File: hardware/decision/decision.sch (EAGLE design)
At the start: 3 parts

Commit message: update schematics
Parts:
- removed LM7805: 7805T, linear:7805T
- removed U$1: LCD-G12864FULL, SparkFun-Displays:LCD-G12864FULL
- added IC1: 7805T, linear:7805T
- added IC2: A1301UA, allegro:A1301UA
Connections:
- removed net P1.0: U$1.RST
- removed net P1.1: U$1.CS1
- removed net P1.4: U$1.DB1
- removed net P1.5: U$1.DB0
- removed net P2.5: U$1.E
- removed net P3.0: U$1.DB7
- removed net P3.1: U$1.DB6
- removed net P3.2: U$1.DB5
- removed net P3.3: U$1.DB4
- removed net P3.4: U$1.DB2
- removed net P4.2: U$1.R/W
- removed net P4.3: U$1.D/I
- removed net P4.7: U$1.DB3
- net GND: now also IC1.GND, IC2.GND; no longer BAT1.V-, LM7805.GND, U$1.K, U$1.VSS
- net N$1: now also IC1.VI; no longer LM7805.VI
- net P1.2: now also IC2.OUT; no longer U$1.CS2
- net VCC: now also IC1.VO, IC2.VCC; no longer LM7805.VO, U$1.A, U$1.VDD, U$1.VEE, U$1.VO
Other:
- note added: "Connects the Hall Effect Sensor to the Green Board and provides the Green Board with power"
- note added: "Derailleurs Decision Board Foster McLane"
- note added: "Hall Effect Sensor"
- note added: "LM7805"
- note removed: "Connects LCD to Green Board and supplies power to the Green Board"
- note removed: "Derailleurs Interface Board Foster McLane"
- note removed: "LCD 128x64"
- note removed: "Power Supply"
- moved on the sheet: BAT1
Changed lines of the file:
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@@
 </classes>
 <parts>
-<part name="U$1" library="SparkFun-Displays" deviceset="LCD-G12864" device="FULL"/>
 <part name="BAT1" library="SparkFun-Connectors" deviceset="BC9VPC" device=""/>
-<part name="LM7805" library="linear" deviceset="78*" device="T" technology="05"/>
+<part name="IC1" library="linear" deviceset="78*" device="T" technology="05"/>
+<part name="IC2" library="allegro" deviceset="A13*?" device="UA" technology="01"/>
 </parts>
 <sheets>
 <sheet>
 <plain>
-<text x="96.52" y="121.92" size="1.778" layer="97">LCD 128x64</text>
-<text x="25.4" y="109.22" size="1.778" layer="97">5V Voltage Regulator</text>
-<text x="-5.08" y="119.38" size="1.778" layer="97">Power Supply</text>
-<frame x1="-20.32" y1="35.56" x2="124.46" y2="154.94" columns="8" rows="5" layer="91"/>
-<text x="-10.16" y="144.78" size="1.778" layer="97">Connects LCD to Green Board and supplies power to the Green Board</text>
-<text x="-10.16" y="139.7" size="1.778" layer="97">This board connects to the Green Board via mated headers.</text>
-<text x="99.06" y="43.18" size="1.778" layer="97">Derailleurs
-Interface Board
+<text x="45.72" y="27.94" size="1.778" layer="97">LM7805</text>
+<frame x1="-2.54" y1="-20.32" x2="96.52" y2="63.5" columns="8" rows="5" layer="91"/>
+<text x="43.18" y="55.88" size="1.778" layer="97">Hall Effect Sensor</text>
+<text x="45.72" y="12.7" size="1.778" layer="97">5V Voltage Regulator</text>
+<text x="5.08" y="-5.08" size="1.778" layer="97">Connects the Hall Effect Sensor to the Green Board and provides
+the Green Board with power</text>
+<text x="5.08" y="-10.16" size="1.778" layer="97">This board connects to the Green Board via mated headers.</text>
+<text x="73.66" y="-15.24" size="1.778" layer="97">Derailleurs
+Decision Board
 Foster McLane</text>
 </plain>
 <instances>
-<instance part="U$1" gate="G$1" x="101.6" y="93.98"/>
-<instance part="BAT1" gate="G$1" x="0" y="96.52"/>
-<instance part="LM7805" gate="A1" x="20.32" y="104.14"/>
+<instance part="BAT1" gate="G$1" x="17.78" y="15.24"/>
+<instance part="IC1" gate="A1" x="43.18" y="22.86"/>
+<instance part="IC2" gate="G$1" x="43.18" y="48.26"/>
 </instances>
 <busses>
 </busses>
 <nets>
-<net name="P2.5" class="0">
+<net name="N$1" class="0">
 <segment>
-<pinref part="U$1" gate="G$1" pin="E"/>
-<wire x1="88.9" y1="76.2" x2="76.2" y2="76.2" width="0.1524" layer="91"/>
-<label x="76.2" y="76.2" size="1.778" layer="95" rot="R180" xref="yes"/>
+<pinref part="BAT1" gate="G$1" pin="V+"/>
+<pinref part="IC1" gate="A1" pin="VI"/>
+<wire x1="17.78" y1="22.86" x2="33.02" y2="22.86" width="0.1524" layer="91"/>
 </segment>
 </net>
-<net name="P4.3" class="0">
+<net name="GND" class="0">
 <segment>
-<pinref part="U$1" gate="G$1" pin="D/I"/>
-<wire x1="88.9" y1="78.74" x2="66.04" y2="78.74" width="0.1524" layer="91"/>
-<label x="66.04" y="78.74" size="1.778" layer="95" rot="R180" xref="yes"/>
+<pinref part="IC1" gate="A1" pin="GND"/>
+<wire x1="43.18" y1="15.24" x2="43.18" y2="5.08" width="0.1524" layer="91"/>
+<wire x1="43.18" y1="5.08" x2="17.78" y2="5.08" width="0.1524" layer="91"/>
+<wire x1="17.78" y1="5.08" x2="17.78" y2="7.62" width="0.1524" layer="91"/>
+<wire x1="43.18" y1="5.08" x2="60.96" y2="5.08" width="0.1524" layer="91"/>
+<label x="60.96" y="5.08" size="1.778" layer="95" xref="yes"/>
+</segment>
+<segment>
+<pinref part="IC2" gate="G$1" pin="GND"/>
+<wire x1="50.8" y1="45.72" x2="68.58" y2="45.72" width="0.1524" layer="91"/>
+<label x="68.58" y="45.72" size="1.778" layer="95" xref="yes"/>
 </segment>
 </net>
-<net name="P4.2" class="0">
+<net name="VCC" class="0">
 <segment>
-<pinref part="U$1" gate="G$1" pin="R/W"/>
-<wire x1="88.9" y1="81.28" x2="76.2" y2="81.28" width="0.1524" layer="91"/>
-<label x="76.2" y="81.28" size="1.778" layer="95" rot="R180" xref="yes"/>
+<pinref part="IC1" gate="A1" pin="VO"/>
+<wire x1="53.34" y1="22.86" x2="60.96" y2="22.86" width="0.1524" layer="91"/>
+<label x="60.96" y="22.86" size="1.778" layer="95" xref="yes"/>
 </segment>
-</net>
-<net name="P1.0" class="0">
 <segment>
-<pinref part="U$1" gate="G$1" pin="RST"/>
-<wire x1="88.9" y1="83.82" x2="66.04" y2="83.82" width="0.1524" layer="91"/>
-<label x="66.04" y="83.82" size="1.778" layer="95" rot="R180" xref="yes"/>
-</segment>
-</net>
-<net name="P1.1" class="0">
-<segment>
-<pinref part="U$1" gate="G$1" pin="CS1"/>
-<wire x1="88.9" y1="86.36" x2="76.2" y2="86.36" width="0.1524" layer="91"/>
-<label x="76.2" y="86.36" size="1.778" layer="95" rot="R180" xref="yes"/>
+<pinref part="IC2" gate="G$1" pin="VCC"/>
+<wire x1="50.8" y1="50.8" x2="68.58" y2="50.8" width="0.1524" layer="91"/>
+<label x="68.58" y="50.8" size="1.778" layer="95" xref="yes"/>
 </segment>
 </net>
 <net name="P1.2" class="0">
 <segment>
-<pinref part="U$1" gate="G$1" pin="CS2"/>
-<wire x1="88.9" y1="88.9" x2="66.04" y2="88.9" width="0.1524" layer="91"/>
-<label x="66.04" y="88.9" size="1.778" layer="95" rot="R180" xref="yes"/>
+<pinref part="IC2" gate="G$1" pin="OUT"/>
+<wire x1="50.8" y1="48.26" x2="58.42" y2="48.26" width="0.1524" layer="91"/>
+<label x="58.42" y="48.26" size="1.778" layer="95" xref="yes"/>
 </segment>
 </net>
-<net name="P3.0" class="0">
-<segment>
-<pinref part="U$1" gate="G$1" pin="DB7"/>
-<wire x1="88.9" y1="91.44" x2="76.2" y2="91.44" width="0.1524" layer="91"/>
-<label x="76.2" y="91.44" size="1.778" layer="95" rot="R180" xref="yes"/>
-</segment>
-</net>
-<net name="P3.1" class="0">
-<segment>
-<pinref part="U$1" gate="G$1" pin="DB6"/>
-<wire x1="88.9" y1="93.98" x2="66.04" y2="93.98" width="0.1524" layer="91"/>
-<label x="66.04" y="93.98" size="1.778" layer="95" rot="R180" xref="yes"/>
-</segment>
-</net>
-<net name="P3.2" class="0">
-<segment>
-<pinref part="U$1" gate="G$1" pin="DB5"/>
-<wire x1="88.9" y1="96.52" x2="76.2" y2="96.52" width="0.1524" layer="91"/>
-<label x="76.2" y="96.52" size="1.778" layer="95" rot="R180" xref="yes"/>
-</segment>
-</net>
-<net name="P3.3" class="0">
-<segment>
-<pinref part="U$1" gate="G$1" pin="DB4"/>
-<wire x1="88.9" y1="99.06" x2="66.04" y2="99.06" width="0.1524" layer="91"/>
-<label x="66.04" y="99.06" size="1.778" layer="95" rot="R180" xref="yes"/>
-</segment>
-</net>
-<net name="P4.7" class="0">
-<segment>
-<pinref part="U$1" gate="G$1" pin="DB3"/>
-<wire x1="88.9" y1="101.6" x2="76.2" y2="101.6" width="0.1524" layer="91"/>
-<label x="76.2" y="101.6" size="1.778" layer="95" rot="R180" xref="yes"/>
-</segment>
-</net>
-<net name="P3.4" class="0">
-<segment>
-<pinref part="U$1" gate="G$1" pin="DB2"/>
-<wire x1="88.9" y1="104.14" x2="66.04" y2="104.14" width="0.1524" layer="91"/>
-<label x="66.04" y="104.14" size="1.778" layer="95" rot="R180" xref="yes"/>
-</segment>
-</net>
-<net name="P1.4" class="0">
-<segment>
-<pinref part="U$1" gate="G$1" pin="DB1"/>
-<wire x1="88.9" y1="106.68" x2="76.2" y2="106.68" width="0.1524" layer="91"/>
-<label x="76.2" y="106.68" size="1.778" layer="95" rot="R180" xref="yes"/>
-</segment>
-</net>
-<net name="P1.5" class="0">
-<segment>
-<pinref part="U$1" gate="G$1" pin="DB0"/>
-<wire x1="88.9" y1="109.22" x2="66.04" y2="109.22" width="0.1524" layer="91"/>
-<label x="66.04" y="109.22" size="1.778" layer="95" rot="R180" xref="yes"/>
-</segment>
-</net>
-<net name="GND" class="0">
-<segment>
-<pinref part="U$1" gate="G$1" pin="VSS"/>
-<label x="66.04" y="114.3" size="1.778" layer="95" rot="R180" xref="yes"/>
-<wire x1="88.9" y1="114.3" x2="66.04" y2="114.3" width="0.1524" layer="91"/>
-</segment>
-<segment>
-<pinref part="U$1" gate="G$1" pin="K"/>
-<wire x1="88.9" y1="68.58" x2="66.04" y2="68.58" width="0.1524" layer="91"/>
-<label x="66.04" y="68.58" size="1.778" layer="95" rot="R180" xref="yes"/>
-</segment>
-<segment>
-<pinref part="LM7805" gate="A1" pin="GND"/>
-<wire x1="20.32" y1="96.52" x2="20.32" y2="83.82" width="0.1524" layer="91"/>
-<pinref part="BAT1" gate="G$1" pin="V-"/>
-<wire x1="20.32" y1="83.82" x2="12.7" y2="83.82" width="0.1524" layer="91"/>
-<wire x1="12.7" y1="83.82" x2="0" y2="83.82" width="0.1524" layer="91"/>
-<wire x1="0" y1="83.82" x2="0" y2="86.36" width="0.1524" layer="91"/>
-<wire x1="12.7" y1="83.82" x2="12.7" y2="88.9" width="0.1524" layer="91"/>
-<label x="12.7" y="88.9" size="1.778" layer="95" rot="R90" xref="yes"/>
-</segment>
-</net>
-<net name="VCC" class="0">
-<segment>
-<pinref part="U$1" gate="G$1" pin="VDD"/>
-<wire x1="88.9" y1="116.84" x2="76.2" y2="116.84" width="0.1524" layer="91"/>
-<label x="76.2" y="116.84" size="1.778" layer="95" rot="R180" xref="yes"/>
-</segment>
-<segment>
-<pinref part="U$1" gate="G$1" pin="VO"/>
-<wire x1="88.9" y1="111.76" x2="76.2" y2="111.76" width="0.1524" layer="91"/>
-<label x="76.2" y="111.76" size="1.778" layer="95" rot="R180" xref="yes"/>
-</segment>
-<segment>
-<pinref part="U$1" gate="G$1" pin="VEE"/>
-<wire x1="88.9" y1="73.66" x2="66.04" y2="73.66" width="0.1524" layer="91"/>
-<label x="66.04" y="73.66" size="1.778" layer="95" rot="R180" xref="yes"/>
-</segment>
-<segment>
-<pinref part="U$1" gate="G$1" pin="A"/>
-<wire x1="88.9" y1="71.12" x2="76.2" y2="71.12" width="0.1524" layer="91"/>
-<label x="76.2" y="71.12" size="1.778" layer="95" rot="R180" xref="yes"/>
-</segment>
-<segment>
-<pinref part="LM7805" gate="A1" pin="VO"/>
-<wire x1="30.48" y1="104.14" x2="38.1" y2="104.14" width="0.1524" layer="91"/>
-<label x="38.1" y="104.14" size="1.778" layer="95" xref="yes"/>
-</segment>
-</net>
-<net name="N$1" class="0">
-<segment>
-<pinref part="BAT1" gate="G$1" pin="V+"/>
-<pinref part="LM7805" gate="A1" pin="VI"/>
-<wire x1="0" y1="104.14" x2="10.16" y2="104.14" width="0.1524" layer="91"/>
-</segment>
-</net>

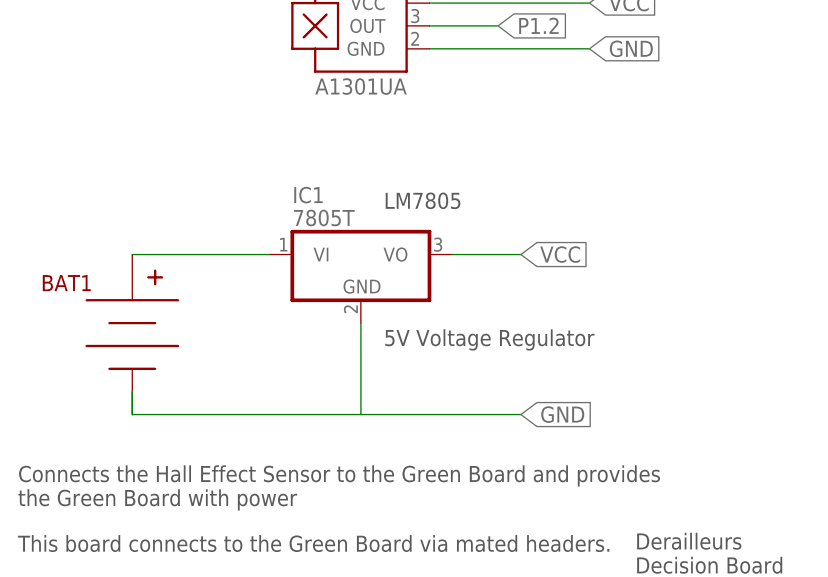
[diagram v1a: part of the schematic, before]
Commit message: add capacitors
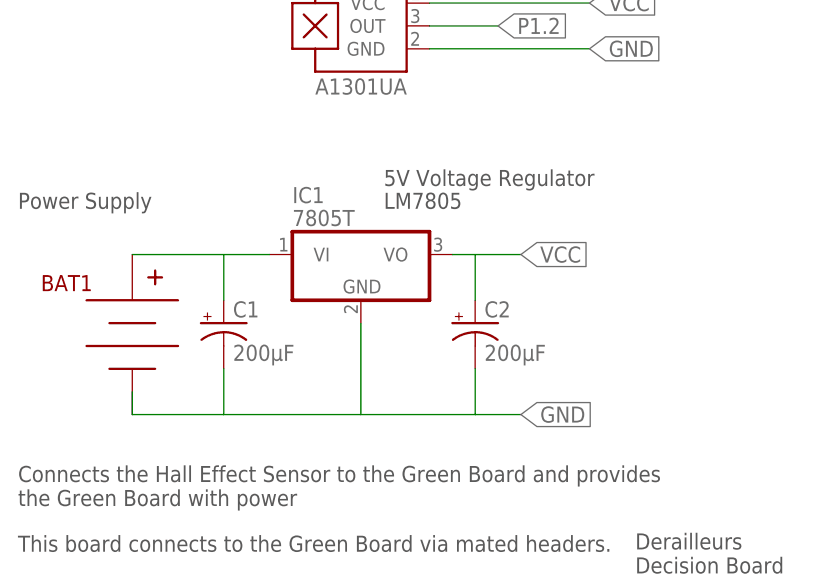
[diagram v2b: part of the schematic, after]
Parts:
- added C1, C2: 200µF, SparkFun-Capacitors:CAP_POLPTH1
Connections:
- net GND: now also C1.-, C2.-
- net N$1: now also C1.+
- net VCC: now also C2.+
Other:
- note added: "Power Supply"
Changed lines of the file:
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@@
 <part name="IC1" library="linear" deviceset="78*" device="T" technology="05"/>
 <part name="IC2" library="allegro" deviceset="A13*?" device="UA" technology="01"/>
+<part name="C1" library="SparkFun-Capacitors" deviceset="CAP_POL" device="PTH1" value="200µF"/>
+<part name="C2" library="SparkFun-Capacitors" deviceset="CAP_POL" device="PTH1" value="200µF"/>
 </parts>
 <sheets>
@@
 <frame x1="-2.54" y1="-20.32" x2="96.52" y2="63.5" columns="8" rows="5" layer="91"/>
 <text x="43.18" y="55.88" size="1.778" layer="97">Hall Effect Sensor</text>
-<text x="45.72" y="12.7" size="1.778" layer="97">5V Voltage Regulator</text>
+<text x="45.72" y="30.48" size="1.778" layer="97">5V Voltage Regulator</text>
 <text x="5.08" y="-5.08" size="1.778" layer="97">Connects the Hall Effect Sensor to the Green Board and provides
 the Green Board with power</text>
@@
 Decision Board
 Foster McLane</text>
+<text x="5.08" y="27.94" size="1.778" layer="97">Power Supply</text>
 </plain>
 <instances>
@@
 <instance part="IC1" gate="A1" x="43.18" y="22.86"/>
 <instance part="IC2" gate="G$1" x="43.18" y="48.26"/>
+<instance part="C1" gate="G$1" x="27.94" y="15.24"/>
+<instance part="C2" gate="G$1" x="55.88" y="15.24"/>
 </instances>
 <busses>
@@
 <pinref part="BAT1" gate="G$1" pin="V+"/>
 <pinref part="IC1" gate="A1" pin="VI"/>
-<wire x1="17.78" y1="22.86" x2="33.02" y2="22.86" width="0.1524" layer="91"/>
+<wire x1="17.78" y1="22.86" x2="27.94" y2="22.86" width="0.1524" layer="91"/>
+<pinref part="C1" gate="G$1" pin="+"/>
+<wire x1="27.94" y1="22.86" x2="33.02" y2="22.86" width="0.1524" layer="91"/>
+<wire x1="27.94" y1="17.78" x2="27.94" y2="22.86" width="0.1524" layer="91"/>
 </segment>
 </net>
@@
 <pinref part="IC1" gate="A1" pin="GND"/>
 <wire x1="43.18" y1="15.24" x2="43.18" y2="5.08" width="0.1524" layer="91"/>
-<wire x1="43.18" y1="5.08" x2="17.78" y2="5.08" width="0.1524" layer="91"/>
+<wire x1="43.18" y1="5.08" x2="27.94" y2="5.08" width="0.1524" layer="91"/>
+<wire x1="27.94" y1="5.08" x2="17.78" y2="5.08" width="0.1524" layer="91"/>
 <wire x1="17.78" y1="5.08" x2="17.78" y2="7.62" width="0.1524" layer="91"/>
-<wire x1="43.18" y1="5.08" x2="60.96" y2="5.08" width="0.1524" layer="91"/>
+<wire x1="43.18" y1="5.08" x2="55.88" y2="5.08" width="0.1524" layer="91"/>
 <label x="60.96" y="5.08" size="1.778" layer="95" xref="yes"/>
+<pinref part="C1" gate="G$1" pin="-"/>
+<wire x1="55.88" y1="5.08" x2="60.96" y2="5.08" width="0.1524" layer="91"/>
+<wire x1="27.94" y1="10.16" x2="27.94" y2="5.08" width="0.1524" layer="91"/>
+<pinref part="C2" gate="G$1" pin="-"/>
+<wire x1="55.88" y1="10.16" x2="55.88" y2="5.08" width="0.1524" layer="91"/>
 </segment>
 <segment>
@@
 <segment>
 <pinref part="IC1" gate="A1" pin="VO"/>
-<wire x1="53.34" y1="22.86" x2="60.96" y2="22.86" width="0.1524" layer="91"/>
+<wire x1="53.34" y1="22.86" x2="55.88" y2="22.86" width="0.1524" layer="91"/>
 <label x="60.96" y="22.86" size="1.778" layer="95" xref="yes"/>
+<pinref part="C2" gate="G$1" pin="+"/>
+<wire x1="55.88" y1="22.86" x2="60.96" y2="22.86" width="0.1524" layer="91"/>
+<wire x1="55.88" y1="17.78" x2="55.88" y2="22.86" width="0.1524" layer="91"/>
 </segment>
 <segment>
